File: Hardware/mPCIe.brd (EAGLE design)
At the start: 100 x 80 mm, 66 parts, among them CN1 MINI_PCIE_1759547-1SMD, J1 SIM_PRT-00548, Q1 BSS138, U1 EDISON_CONNECTOR_FULLMOUNTING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, U2 USB2512BQFN, U3 BA33DD0WHFPSMD, U4 FT231XS-U, U5 TPS62065, U7 BA15BC0FP-E2, Y1 24MHz 50ppm

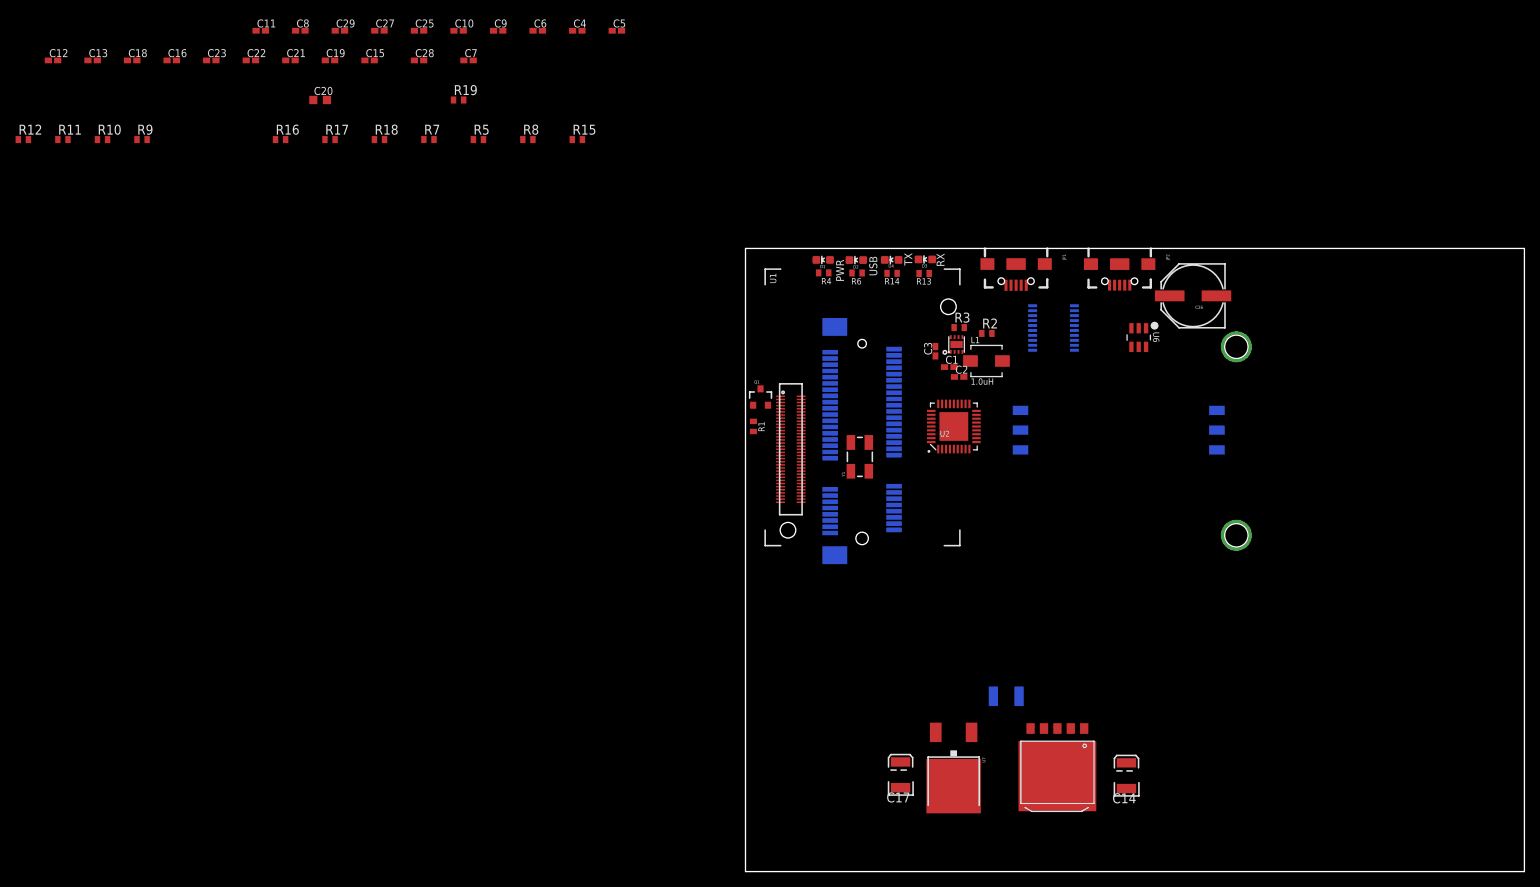
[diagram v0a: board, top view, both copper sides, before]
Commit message: moved all components onto layout; grouped by major function
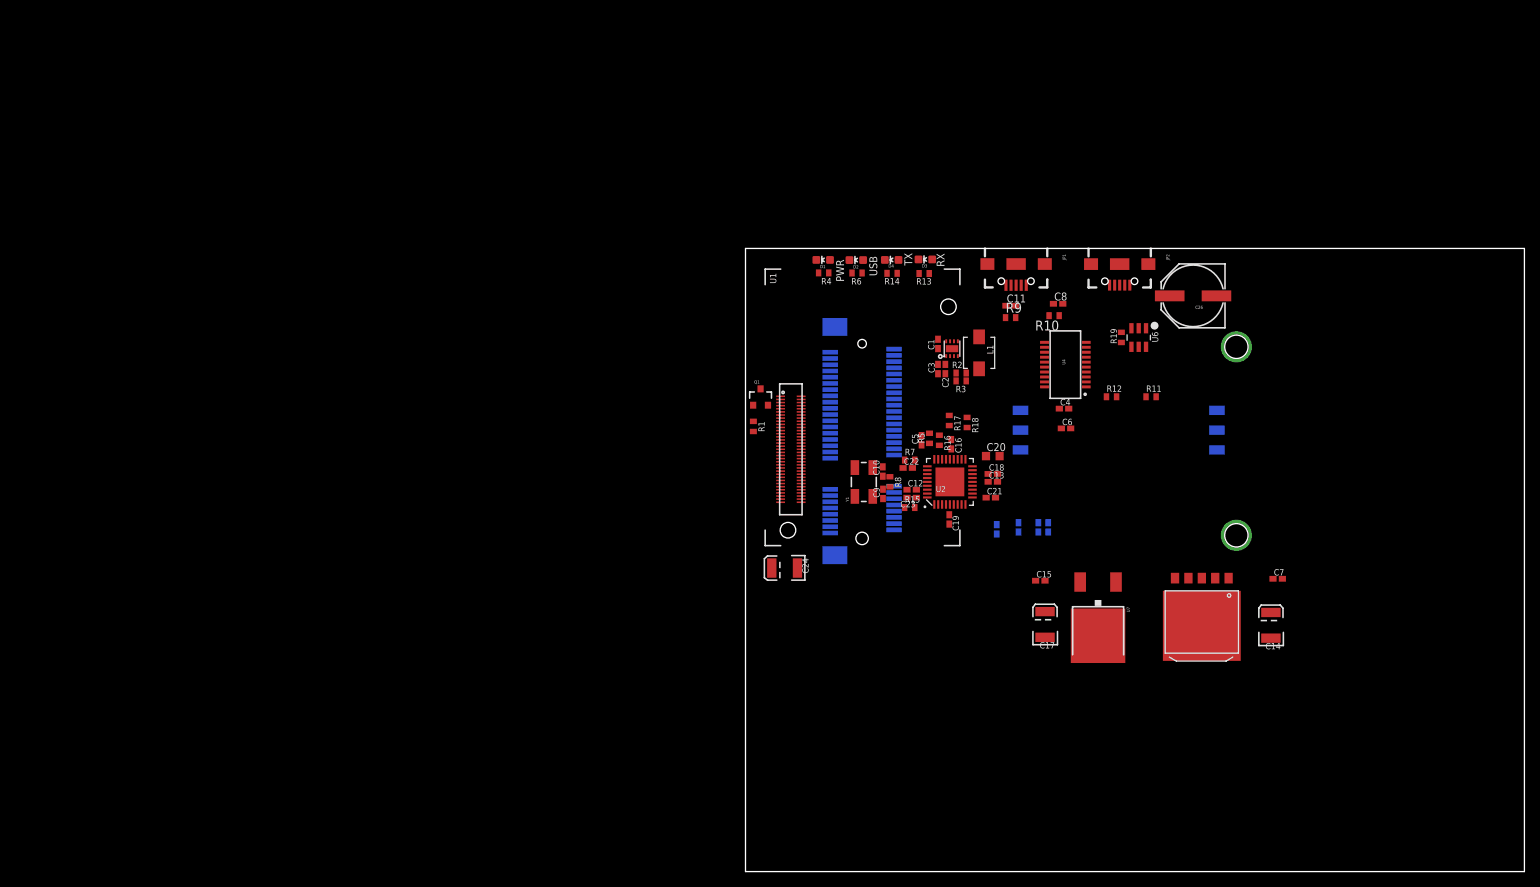
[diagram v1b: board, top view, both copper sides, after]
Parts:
- L1: value 1.0uH -> (none)
- moved R11 143.5 mm to (52.1, 61.0)
- moved R12 143.5 mm to (47.0, 61.0)
- moved C13 127.6 mm to (31.8, 50.0)
- moved R10 124.2 mm to (39.6, 71.4), turned to 180 degrees
- moved C7 123.4 mm to (68.3, 37.6)
- moved C12 123.2 mm to (21.3, 49.0)
- moved C18 122.6 mm to (31.8, 51.1)
- moved R9 113.8 mm to (34.0, 71.1)
- moved C16 111.5 mm to (26.4, 54.9), turned to 90 degrees
- moved C29 111.1 mm to (38.9, 44.2), flipped to the bottom, turned to 90 degrees
- moved C15 109.0 mm to (37.8, 37.3)
- moved C21 106.0 mm to (31.5, 48.0)
- moved C23 106.0 mm to (21.3, 48.0), turned to 180 degrees
- moved C27 103.9 mm to (35.1, 44.2), flipped to the bottom, turned to 270 degrees
- moved C8 103.4 mm to (40.1, 72.9)
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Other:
- board text added: "Designed by Parker Lusk"
- board text added: "mPCIe Block rev .01"

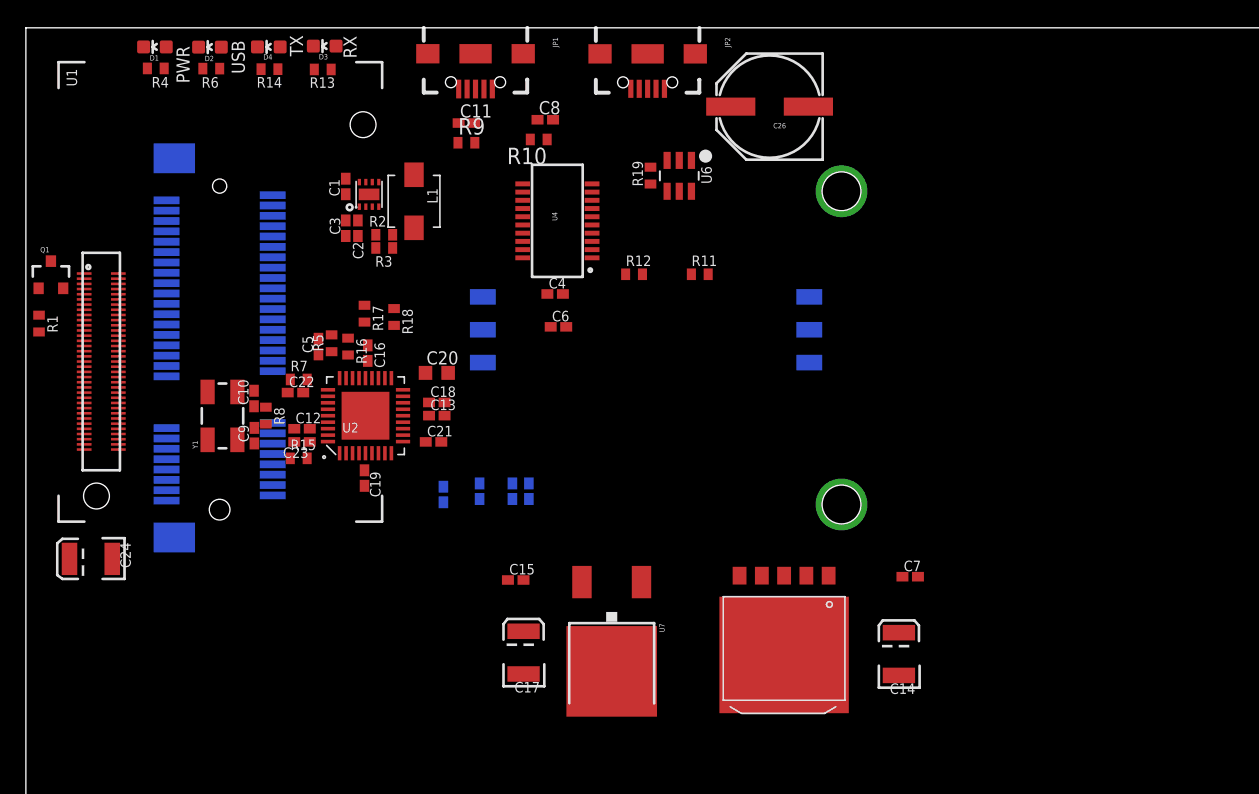
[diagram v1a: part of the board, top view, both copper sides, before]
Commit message: v0.3 of schematic: connected all the 3.3v nets to PSUs and not Edison; removed tantalum caps; replaced LDO Vout caps with MLCCs and series ESRs; laid out board and ready to route
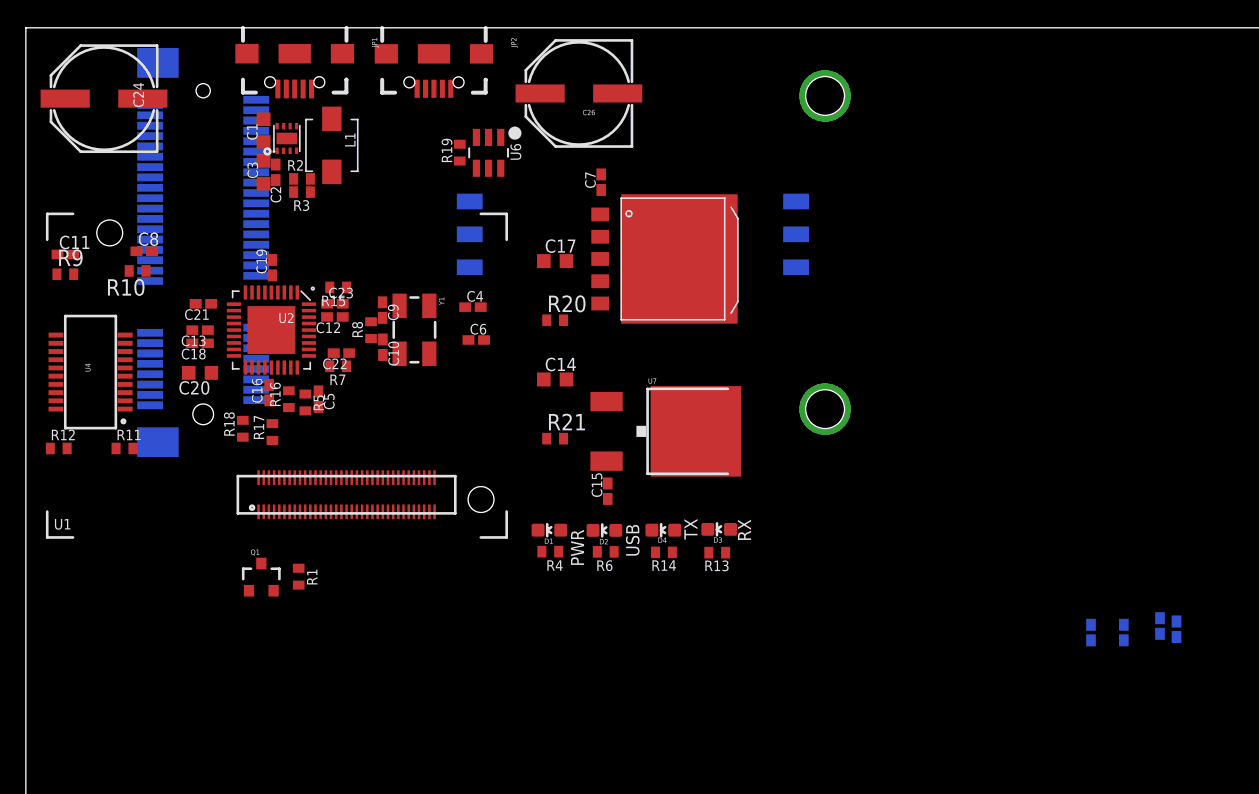
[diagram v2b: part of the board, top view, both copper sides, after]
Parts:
- added R20, R21: 1 Ohm, rcl:R0402
- C1, C3: device rcl:C0402K -> rcl:C0603K
- C14, C17: value 22uF TANT -> 22uF; device SparkFun-Capacitors:EIA3528 -> rcl:C0603K
- C24: value 470uF TANT -> 470uF; device SparkFun-Capacitors:EIA3528 -> SparkFun-Capacitors:PANASONIC_E
- moved C25 51.2 mm to (82.3, 33.3)
- moved C29 51.2 mm to (88.9, 33.5)
- moved C28 51.1 mm to (87.6, 33.8)
- moved C27 51.0 mm to (84.8, 33.3)
- moved D1 48.2 mm to (40.5, 41.2)
- moved R13 48.2 mm to (53.4, 39.4)
- moved D4 48.2 mm to (49.2, 41.2)
- moved R14 48.2 mm to (49.3, 39.5)
- moved R4 48.2 mm to (40.5, 39.5)
- moved R6 48.2 mm to (44.8, 39.5)
- moved D2 48.2 mm to (44.7, 41.2)
- moved D3 48.2 mm to (53.6, 41.2)
- moved R11 46.4 mm to (7.62, 47.5)
- moved R12 46.4 mm to (2.54, 47.5)
- moved C7 38.7 mm to (44.5, 68.1), turned to 90 degrees
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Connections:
- removed net 3.3V_2A: C14.A, C24.A, CN1.2, CN1.24, CN1.39, CN1.41, CN1.52, U3.4
- new net N$16: C17.1, R20.1
- new net N$21: C14.1, R21.1
- new net P$1: R20.2, U7.3
- net 1.5V: no longer C17.A, U7.3
- net 3.3V: now also C24.+, CN1.2, CN1.24, CN1.39, CN1.41, CN1.52, R21.2, U3.4; no longer U1.10, U1.8
- net GND: now also C14.2, C17.2, C24.-; no longer C14.C, C17.C, C24.C
